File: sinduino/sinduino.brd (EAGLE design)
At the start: 100 x 80 mm, 34 parts, among them IC1 IC_UC_ATMEGA32U4-TQFP44, IC2 TS2940CT5TV, Q1 16000, X1 MINI-USB-32005-301

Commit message: proceed routing
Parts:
- moved LED3 5.02 mm to (53.7, 14.9)
- moved R4 3.19 mm to (52.4, 10.8)
- moved R5 1.91 mm to (47.0, 10.5)
- moved C5 0.71 mm to (42.9, 8.57), turned to 0 degrees
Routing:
- net D13: track 21.8 -> 7.88 mm
- net VCC: track 98.9 -> 103.9 mm
- net HWB: track 2.81 -> 4.71 mm
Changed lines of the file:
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@@
 <element name="C3" library="rcl" package="C1206" value="100n" x="36.195" y="24.765" rot="MR180"/>
 <element name="C4" library="rcl" package="C1206" value="100n" x="55.245" y="23.495" rot="MR0"/>
-<element name="C5" library="rcl" package="C1206" value="100n" x="42.545" y="9.2075" rot="MR270"/>
+<element name="C5" library="rcl" package="C1206" value="100n" x="42.8625" y="8.5725" rot="MR0"/>
 <element name="C6" library="rcl" package="C1206" value="100n" x="24.13" y="10.4775" rot="MR0"/>
 <element name="C7" library="rcl" package="C1206" value="100n" x="22.5425" y="7.62" rot="MR0"/>
@@
 <element name="R6" library="rcl" package="R1206" value="680" x="50.165" y="20.32" rot="MR0"/>
 <element name="LED4" library="led" package="LED3MM" value="yellow" x="55.245" y="27.305" rot="R180"/>
-<element name="R5" library="rcl" package="R1206" value="3k9" x="45.085" y="10.4775" rot="MR90"/>
+<element name="R5" library="rcl" package="R1206" value="3k9" x="46.99" y="10.4775" rot="MR90"/>
 <element name="IC2" library="n39" package="TO220V" value="TS2940CT5TV" x="20.32" y="25.0825" rot="R270">
 <attribute name="REICHELT" value="LM 2940 CT5" x="20.32" y="25.0825" size="1.778" layer="27" rot="R270" display="off"/>
@@
 <element name="R2" library="rcl" package="R1206" value="680" x="18.415" y="30.1625" rot="MR0"/>
 <element name="LED2" library="led" package="LED3MM" value="orange" x="22.86" y="27.305" rot="R270"/>
-<element name="R4" library="rcl" package="R1206" value="680" x="49.2125" y="10.4775" rot="MR0"/>
-<element name="LED3" library="led" package="LED3MM" value="red" x="48.895" y="13.335"/>
+<element name="R4" library="rcl" package="R1206" value="680" x="52.3875" y="10.795" rot="MR0"/>
+<element name="LED3" library="led" package="LED3MM" value="red" x="53.6575" y="14.9225"/>
 </elements>
 <signals>
@@
 <wire x1="41.3" y1="19.71" x2="40.83" y2="19.24" width="0.4064" layer="16"/>
 <wire x1="40.83" y1="10.81" x2="40.83" y2="19.24" width="0.4064" layer="16"/>
+<wire x1="44.2625" y1="8.5725" x2="44.2625" y2="9.7125" width="0.4064" layer="16"/>
+<wire x1="40.83" y1="10.81" x2="43.165" y2="10.81" width="0.4064" layer="16"/>
+<wire x1="43.165" y1="10.81" x2="44.2625" y2="9.7125" width="0.4064" layer="16"/>
 <wire x1="56.645" y1="23.495" x2="56.515" y2="27.305" width="0" layer="19" extent="16-16"/>
 <wire x1="42.53" y1="19.71" x2="56.645" y2="23.495" width="0" layer="19" extent="16-16"/>
-<wire x1="42.545" y1="10.6075" x2="40.83" y2="10.81" width="0" layer="19" extent="16-16"/>
 <wire x1="34.43" y1="19.5075" x2="40.83" y2="19.24" width="0" layer="19" extent="16-16"/>
 <wire x1="34.795" y1="24.765" x2="34.43" y2="22.21" width="0" layer="19" extent="16-16"/>
@@
 <contactref element="LED3" pad="A"/>
 <wire x1="42.53" y1="13.31" x2="47.6" y2="13.31" width="0.4064" layer="16"/>
-<wire x1="47.6" y1="13.31" x2="47.625" y2="13.335" width="0.4064" layer="16"/>
+<wire x1="47.6" y1="13.31" x2="52.3875" y2="14.9225" width="0" layer="19" extent="1-16"/>
 <wire x1="40.16" y1="4" x2="40.16" y2="5.235" width="0.4064" layer="16"/>
 <wire x1="40.16" y1="5.235" x2="41.275" y2="6.35" width="0.4064" layer="16"/>
-<wire x1="41.275" y1="6.35" x2="45.085" y2="6.35" width="0.4064" layer="16"/>
-<wire x1="45.085" y1="6.35" x2="47.3075" y2="8.5725" width="0.4064" layer="16"/>
-<wire x1="47.3075" y1="8.5725" x2="48.5775" y2="8.5725" width="0.4064" layer="16"/>
-<wire x1="48.5775" y1="8.5725" x2="49.2125" y2="9.2075" width="0.4064" layer="16"/>
-<wire x1="49.2125" y1="9.2075" x2="49.2125" y2="11.7475" width="0.4064" layer="16"/>
-<wire x1="49.2125" y1="11.7475" x2="47.625" y2="13.335" width="0.4064" layer="16"/>
+<wire x1="48.5775" y1="8.5725" x2="49.2125" y2="9.2075" width="0" layer="19" extent="1-16"/>
+<wire x1="49.2125" y1="9.2075" x2="49.2125" y2="11.7475" width="0" layer="19" extent="1-16"/>
+<wire x1="49.2125" y1="11.7475" x2="52.3875" y2="14.9225" width="0" layer="19" extent="1-16"/>
+<wire x1="41.275" y1="6.35" x2="42.53" y2="13.31" width="0" layer="19" extent="16-16"/>
 </signal>
 <signal name="D5">
@@
 <contactref element="R5" pad="2"/>
 <wire x1="42.53" y1="12.51" x2="43.6875" y2="12.51" width="0.4064" layer="16"/>
-<wire x1="45.085" y1="11.8995" x2="44.298" y2="11.8995" width="0.4064" layer="16"/>
+<wire x1="46.99" y1="11.8995" x2="44.298" y2="11.8995" width="0.4064" layer="16"/>
 <wire x1="44.298" y1="11.8995" x2="43.6875" y2="12.51" width="0.4064" layer="16"/>
 </signal>
@@
 <contactref element="LED3" pad="K"/>
 <contactref element="R4" pad="1"/>
-<wire x1="50.6345" y1="10.4775" x2="50.165" y2="13.335" width="0" layer="19" extent="16-16"/>
+<wire x1="53.8095" y1="10.795" x2="54.9275" y2="14.9225" width="0" layer="19" extent="16-16"/>
 </signal>
 </signals>

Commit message: route lower right part
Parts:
- moved LED3 3.55 mm to (50.5, 13.3)
- moved R4 1.93 mm to (50.5, 10.5)
- moved R5 0.32 mm to (46.7, 10.5)
- moved C5 0.32 mm to (42.9, 8.89), turned to 180 degrees
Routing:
- net D5: track 0.00 -> 29.2 mm
- net N$1: track 0.00 -> 28.5 mm
- net N$12: track 0.00 -> 27.8 mm
- net N$13: track 0.00 -> 27.1 mm
- net D13: track 7.88 -> 24.5 mm
- net VCC: track 103.9 -> 101.1 mm
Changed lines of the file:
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@@
 <element name="C3" library="rcl" package="C1206" value="100n" x="36.195" y="24.765" rot="MR180"/>
 <element name="C4" library="rcl" package="C1206" value="100n" x="55.245" y="23.495" rot="MR0"/>
-<element name="C5" library="rcl" package="C1206" value="100n" x="42.8625" y="8.5725" rot="MR0"/>
+<element name="C5" library="rcl" package="C1206" value="100n" x="42.8625" y="8.89" rot="MR180"/>
 <element name="C6" library="rcl" package="C1206" value="100n" x="24.13" y="10.4775" rot="MR0"/>
 <element name="C7" library="rcl" package="C1206" value="100n" x="22.5425" y="7.62" rot="MR0"/>
@@
 <element name="R6" library="rcl" package="R1206" value="680" x="50.165" y="20.32" rot="MR0"/>
 <element name="LED4" library="led" package="LED3MM" value="yellow" x="55.245" y="27.305" rot="R180"/>
-<element name="R5" library="rcl" package="R1206" value="3k9" x="46.99" y="10.4775" rot="MR90"/>
+<element name="R5" library="rcl" package="R1206" value="3k9" x="46.6725" y="10.4775" rot="MR90"/>
 <element name="IC2" library="n39" package="TO220V" value="TS2940CT5TV" x="20.32" y="25.0825" rot="R270">
 <attribute name="REICHELT" value="LM 2940 CT5" x="20.32" y="25.0825" size="1.778" layer="27" rot="R270" display="off"/>
@@
 <element name="R2" library="rcl" package="R1206" value="680" x="18.415" y="30.1625" rot="MR0"/>
 <element name="LED2" library="led" package="LED3MM" value="orange" x="22.86" y="27.305" rot="R270"/>
-<element name="R4" library="rcl" package="R1206" value="680" x="52.3875" y="10.795" rot="MR0"/>
-<element name="LED3" library="led" package="LED3MM" value="red" x="53.6575" y="14.9225"/>
+<element name="R4" library="rcl" package="R1206" value="680" x="50.4825" y="10.4775" rot="MR0"/>
+<element name="LED3" library="led" package="LED3MM" value="red" x="50.4825" y="13.335"/>
 </elements>
 <signals>
@@
 <wire x1="41.3" y1="19.71" x2="40.83" y2="19.24" width="0.4064" layer="16"/>
 <wire x1="40.83" y1="10.81" x2="40.83" y2="19.24" width="0.4064" layer="16"/>
-<wire x1="44.2625" y1="8.5725" x2="44.2625" y2="9.7125" width="0.4064" layer="16"/>
-<wire x1="40.83" y1="10.81" x2="43.165" y2="10.81" width="0.4064" layer="16"/>
-<wire x1="43.165" y1="10.81" x2="44.2625" y2="9.7125" width="0.4064" layer="16"/>
+<wire x1="40.83" y1="10.81" x2="40.83" y2="9.5225" width="0.4064" layer="16"/>
+<wire x1="40.83" y1="9.5225" x2="41.4625" y2="8.89" width="0.4064" layer="16"/>
 <wire x1="56.645" y1="23.495" x2="56.515" y2="27.305" width="0" layer="19" extent="16-16"/>
 <wire x1="42.53" y1="19.71" x2="56.645" y2="23.495" width="0" layer="19" extent="16-16"/>
@@
 <contactref element="JP3" pad="5"/>
 <contactref element="LED3" pad="A"/>
-<wire x1="42.53" y1="13.31" x2="47.6" y2="13.31" width="0.4064" layer="16"/>
-<wire x1="47.6" y1="13.31" x2="52.3875" y2="14.9225" width="0" layer="19" extent="1-16"/>
-<wire x1="40.16" y1="4" x2="40.16" y2="5.235" width="0.4064" layer="16"/>
-<wire x1="40.16" y1="5.235" x2="41.275" y2="6.35" width="0.4064" layer="16"/>
-<wire x1="48.5775" y1="8.5725" x2="49.2125" y2="9.2075" width="0" layer="19" extent="1-16"/>
-<wire x1="49.2125" y1="9.2075" x2="49.2125" y2="11.7475" width="0" layer="19" extent="1-16"/>
-<wire x1="49.2125" y1="11.7475" x2="52.3875" y2="14.9225" width="0" layer="19" extent="1-16"/>
-<wire x1="41.275" y1="6.35" x2="42.53" y2="13.31" width="0" layer="19" extent="16-16"/>
+<wire x1="40.16" y1="4" x2="40.16" y2="5.235" width="0.3048" layer="16"/>
+<wire x1="43.4975" y1="6.985" x2="42.8625" y2="6.35" width="0.3048" layer="16"/>
+<wire x1="42.8625" y1="6.35" x2="41.275" y2="6.35" width="0.3048" layer="16"/>
+<wire x1="41.275" y1="6.35" x2="40.16" y2="5.235" width="0.3048" layer="16"/>
+<wire x1="45.72" y1="7.62" x2="45.085" y2="6.985" width="0.3048" layer="16"/>
+<wire x1="45.085" y1="6.985" x2="43.4975" y2="6.985" width="0.3048" layer="16"/>
+<wire x1="50.165" y1="8.89" x2="50.4825" y2="9.2075" width="0.3048" layer="16"/>
+<wire x1="50.4825" y1="9.2075" x2="50.4825" y2="12.065" width="0.3048" layer="16"/>
+<wire x1="50.4825" y1="12.065" x2="49.2125" y2="13.335" width="0.3048" layer="16"/>
+<wire x1="42.53" y1="13.31" x2="49.1875" y2="13.31" width="0.4064" layer="16"/>
+<wire x1="49.1875" y1="13.31" x2="49.2125" y2="13.335" width="0.4064" layer="16"/>
+<wire x1="45.72" y1="7.62" x2="48.26" y2="7.62" width="0.3048" layer="16"/>
+<wire x1="50.165" y1="8.89" x2="49.53" y2="8.89" width="0.3048" layer="16"/>
+<wire x1="49.53" y1="8.89" x2="48.26" y2="7.62" width="0.3048" layer="16"/>
 </signal>
 <signal name="D5">
 <contactref element="IC1" pad="P31"/>
 <contactref element="JP3" pad="4"/>
-<wire x1="42.7" y1="4" x2="42.53" y2="14.11" width="0" layer="19" extent="16-16"/>
+<wire x1="42.7" y1="4" x2="42.7" y2="5.235" width="0.3048" layer="16"/>
+<wire x1="42.7" y1="5.235" x2="43.815" y2="6.35" width="0.3048" layer="16"/>
+<wire x1="46.0375" y1="6.985" x2="45.4025" y2="6.35" width="0.3048" layer="16"/>
+<wire x1="45.4025" y1="6.35" x2="43.815" y2="6.35" width="0.3048" layer="16"/>
+<wire x1="50.4825" y1="8.255" x2="51.1175" y2="8.89" width="0.3048" layer="16"/>
+<wire x1="51.1175" y1="8.89" x2="52.705" y2="8.89" width="0.3048" layer="16"/>
+<wire x1="52.705" y1="8.89" x2="53.34" y2="9.525" width="0.3048" layer="16"/>
+<wire x1="53.34" y1="9.525" x2="53.34" y2="13.6525" width="0.3048" layer="16"/>
+<wire x1="53.34" y1="13.6525" x2="52.3875" y2="14.605" width="0.3048" layer="16"/>
+<wire x1="42.53" y1="14.11" x2="48.0825" y2="14.11" width="0.3048" layer="16"/>
+<wire x1="48.0825" y1="14.11" x2="48.5775" y2="14.605" width="0.3048" layer="16"/>
+<wire x1="48.5775" y1="14.605" x2="52.3875" y2="14.605" width="0.3048" layer="16"/>
+<wire x1="46.0375" y1="6.985" x2="48.5775" y2="6.985" width="0.3048" layer="16"/>
+<wire x1="50.4825" y1="8.255" x2="49.8475" y2="8.255" width="0.3048" layer="16"/>
+<wire x1="49.8475" y1="8.255" x2="48.5775" y2="6.985" width="0.3048" layer="16"/>
 </signal>
 <signal name="N$1">
 <contactref element="JP3" pad="3"/>
 <contactref element="IC1" pad="P30"/>
-<wire x1="45.24" y1="4" x2="42.53" y2="14.91" width="0" layer="19" extent="16-16"/>
+<wire x1="45.24" y1="4" x2="45.24" y2="5.235" width="0.3048" layer="16"/>
+<wire x1="45.24" y1="5.235" x2="46.355" y2="6.35" width="0.3048" layer="16"/>
+<wire x1="50.8" y1="7.62" x2="51.435" y2="8.255" width="0.3048" layer="16"/>
+<wire x1="51.435" y1="8.255" x2="53.0225" y2="8.255" width="0.3048" layer="16"/>
+<wire x1="53.0225" y1="8.255" x2="53.975" y2="9.2075" width="0.3048" layer="16"/>
+<wire x1="53.975" y1="9.2075" x2="53.975" y2="13.97" width="0.3048" layer="16"/>
+<wire x1="42.53" y1="14.91" x2="47.93" y2="14.91" width="0.3048" layer="16"/>
+<wire x1="47.93" y1="14.91" x2="48.26" y2="15.24" width="0.3048" layer="16"/>
+<wire x1="48.26" y1="15.24" x2="52.705" y2="15.24" width="0.3048" layer="16"/>
+<wire x1="52.705" y1="15.24" x2="53.975" y2="13.97" width="0.3048" layer="16"/>
+<wire x1="46.355" y1="6.35" x2="48.895" y2="6.35" width="0.3048" layer="16"/>
+<wire x1="50.8" y1="7.62" x2="50.165" y2="7.62" width="0.3048" layer="16"/>
+<wire x1="48.895" y1="6.35" x2="50.165" y2="7.62" width="0.3048" layer="16"/>
 </signal>
 <signal name="N$12">
 <contactref element="IC1" pad="P29"/>
 <contactref element="JP3" pad="2"/>
-<wire x1="47.78" y1="4" x2="42.53" y2="15.71" width="0" layer="19" extent="16-16"/>
+<wire x1="47.78" y1="4" x2="47.78" y2="5.235" width="0.3048" layer="16"/>
+<wire x1="47.78" y1="5.235" x2="48.26" y2="5.715" width="0.3048" layer="16"/>
+<wire x1="51.1175" y1="6.985" x2="51.7525" y2="7.62" width="0.3048" layer="16"/>
+<wire x1="51.7525" y1="7.62" x2="53.34" y2="7.62" width="0.3048" layer="16"/>
+<wire x1="53.34" y1="7.62" x2="54.61" y2="8.89" width="0.3048" layer="16"/>
+<wire x1="54.61" y1="8.89" x2="54.61" y2="14.2875" width="0.3048" layer="16"/>
+<wire x1="42.53" y1="15.71" x2="47.7775" y2="15.71" width="0.3048" layer="16"/>
+<wire x1="47.7775" y1="15.71" x2="47.9425" y2="15.875" width="0.3048" layer="16"/>
+<wire x1="47.9425" y1="15.875" x2="53.0225" y2="15.875" width="0.3048" layer="16"/>
+<wire x1="53.0225" y1="15.875" x2="54.61" y2="14.2875" width="0.3048" layer="16"/>
+<wire x1="48.26" y1="5.715" x2="49.2125" y2="5.715" width="0.3048" layer="16"/>
+<wire x1="51.1175" y1="6.985" x2="50.4825" y2="6.985" width="0.3048" layer="16"/>
+<wire x1="49.2125" y1="5.715" x2="50.4825" y2="6.985" width="0.3048" layer="16"/>
 </signal>
 <signal name="N$13">
 <contactref element="JP3" pad="1"/>
 <contactref element="IC1" pad="P28"/>
-<wire x1="50.32" y1="4" x2="42.53" y2="16.51" width="0" layer="19" extent="16-16"/>
+<wire x1="50.32" y1="4" x2="50.32" y2="5.235" width="0.3048" layer="16"/>
+<wire x1="50.32" y1="5.235" x2="52.07" y2="6.985" width="0.3048" layer="16"/>
+<wire x1="52.07" y1="6.985" x2="53.6575" y2="6.985" width="0.3048" layer="16"/>
+<wire x1="53.6575" y1="6.985" x2="55.245" y2="8.5725" width="0.3048" layer="16"/>
+<wire x1="42.53" y1="16.51" x2="53.34" y2="16.51" width="0.3048" layer="16"/>
+<wire x1="53.34" y1="16.51" x2="55.245" y2="14.605" width="0.3048" layer="16"/>
+<wire x1="55.245" y1="14.605" x2="55.245" y2="8.5725" width="0.3048" layer="16"/>
 </signal>
 <signal name="HWB">
@@
 <contactref element="R5" pad="2"/>
 <wire x1="42.53" y1="12.51" x2="43.6875" y2="12.51" width="0.4064" layer="16"/>
-<wire x1="46.99" y1="11.8995" x2="44.298" y2="11.8995" width="0.4064" layer="16"/>
+<wire x1="46.6725" y1="11.8995" x2="44.298" y2="11.8995" width="0.4064" layer="16"/>
 <wire x1="44.298" y1="11.8995" x2="43.6875" y2="12.51" width="0.4064" layer="16"/>
 </signal>
@@
 <contactref element="LED3" pad="K"/>
 <contactref element="R4" pad="1"/>
-<wire x1="53.8095" y1="10.795" x2="54.9275" y2="14.9225" width="0" layer="19" extent="16-16"/>
+<wire x1="51.9045" y1="10.4775" x2="51.7525" y2="13.335" width="0" layer="19" extent="16-16"/>
 </signal>
 </signals>

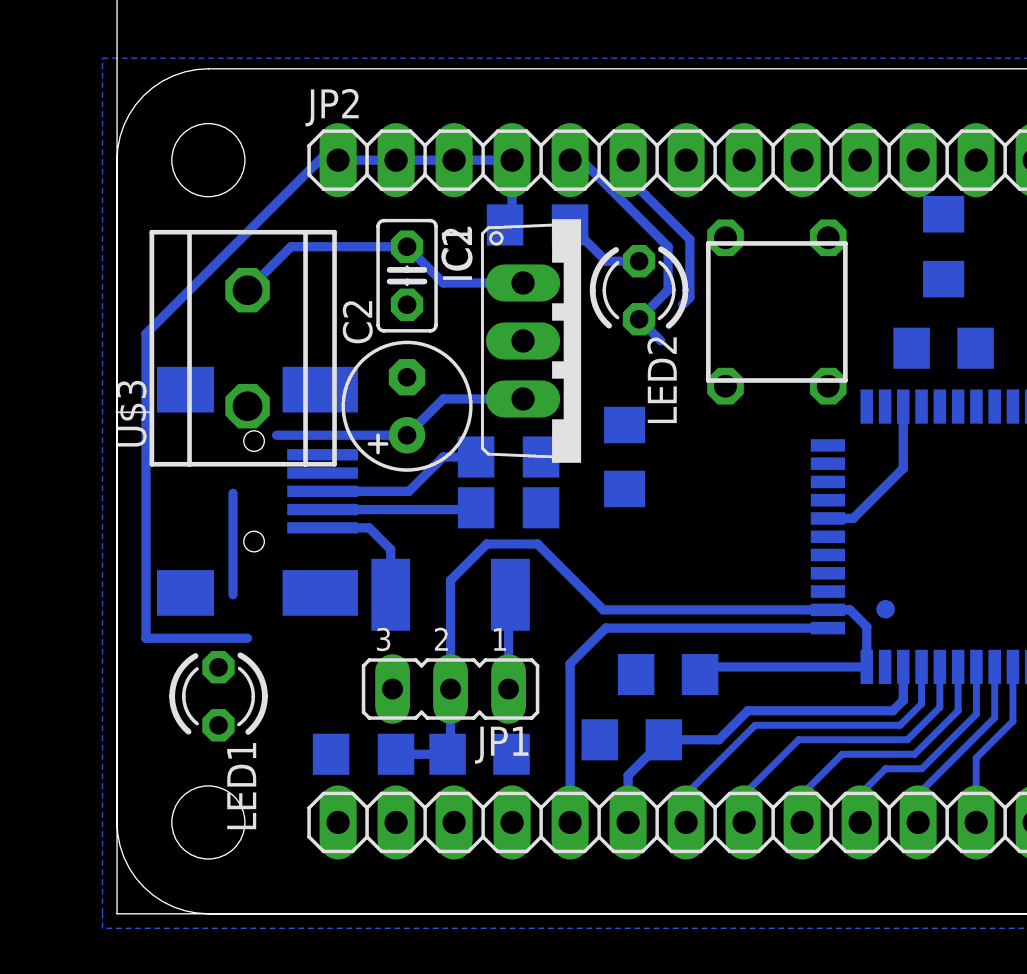
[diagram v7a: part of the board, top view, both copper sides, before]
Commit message: route left part of the board
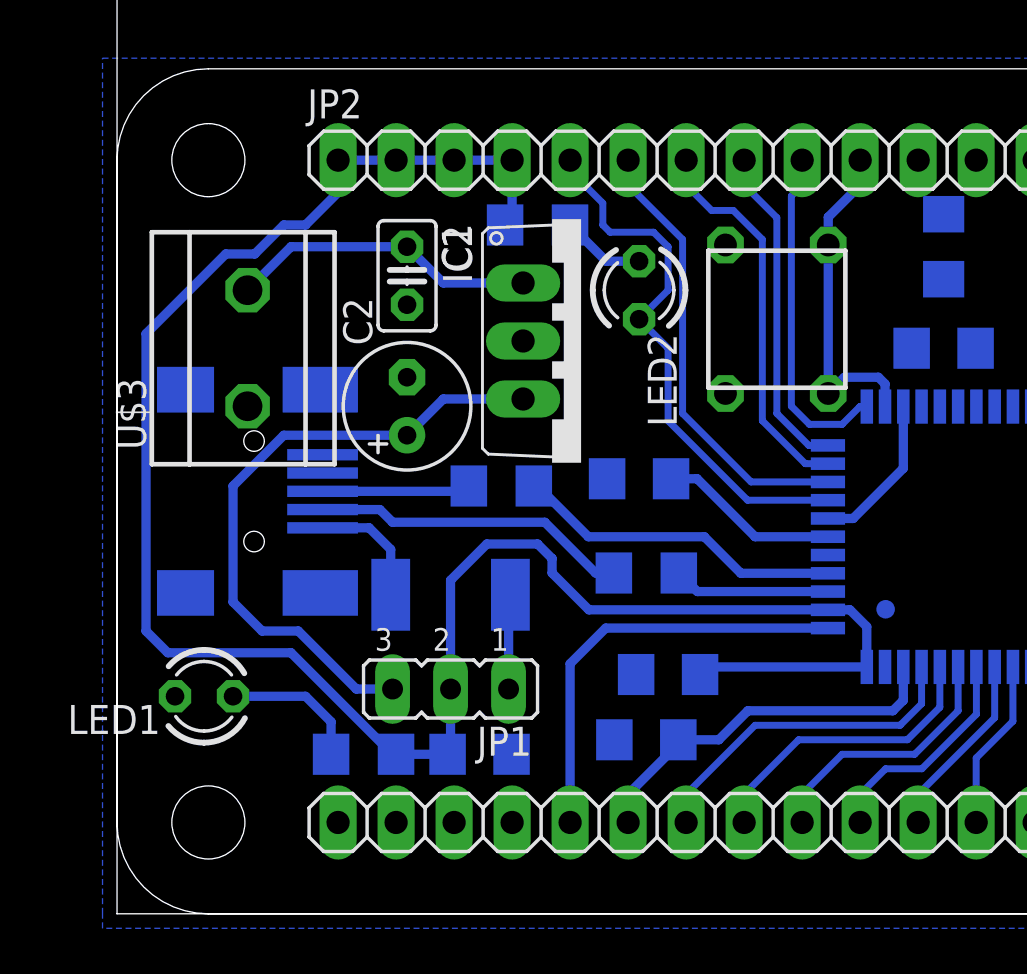
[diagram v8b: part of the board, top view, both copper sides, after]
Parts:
- moved R7 6.68 mm to (23.2, 14.9)
- moved R8 1.31 mm to (16.8, 18.7)
- moved C10 1.14 mm to (22.9, 19.1), turned to 0 degrees
- moved LED1 0.64 mm to (3.81, 9.53), turned to 180 degrees
- moved C7 0.63 mm to (23.2, 7.62)
- moved U$1 0.32 mm to (28.9, 26.0)
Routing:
- net D16: track 0.00 -> 17.0 mm
- net D11: track 0.00 -> 14.9 mm
- net !RESET: track 0.00 -> 14.7 mm
- net D17: track 0.00 -> 14.5 mm
- net N$8: track 0.00 -> 14.5 mm
- net D14: track 11.6 -> 23.8 mm
- net D15: track 7.58 -> 19.7 mm
- net N$16: track 15.9 -> 27.9 mm
- net VCC: track 101.1 -> 109.5 mm
- net N$6: track 0.00 -> 7.92 mm
- net N$5: track 6.76 -> 13.9 mm
- net N$9: track 0.15 -> 6.87 mm
- net N$14: track 0.00 -> 6.18 mm
- net N$7: track 7.35 -> 6.50 mm
